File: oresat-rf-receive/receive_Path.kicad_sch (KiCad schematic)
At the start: 32 parts, among them J11 142-0711-201, J12 0022232021, J13 0022232021, J15 0022232041, J8 142-0711-201, U18 PAT1220-C-3DB, U23 PAT1220-C-3DB, U24 TQP3M9037, U25 PD2328J5050S2HF, U26 TQP3M9037, U27 LTC5505-1ES5, U28 SN74LVC1G32QDBVRQ1

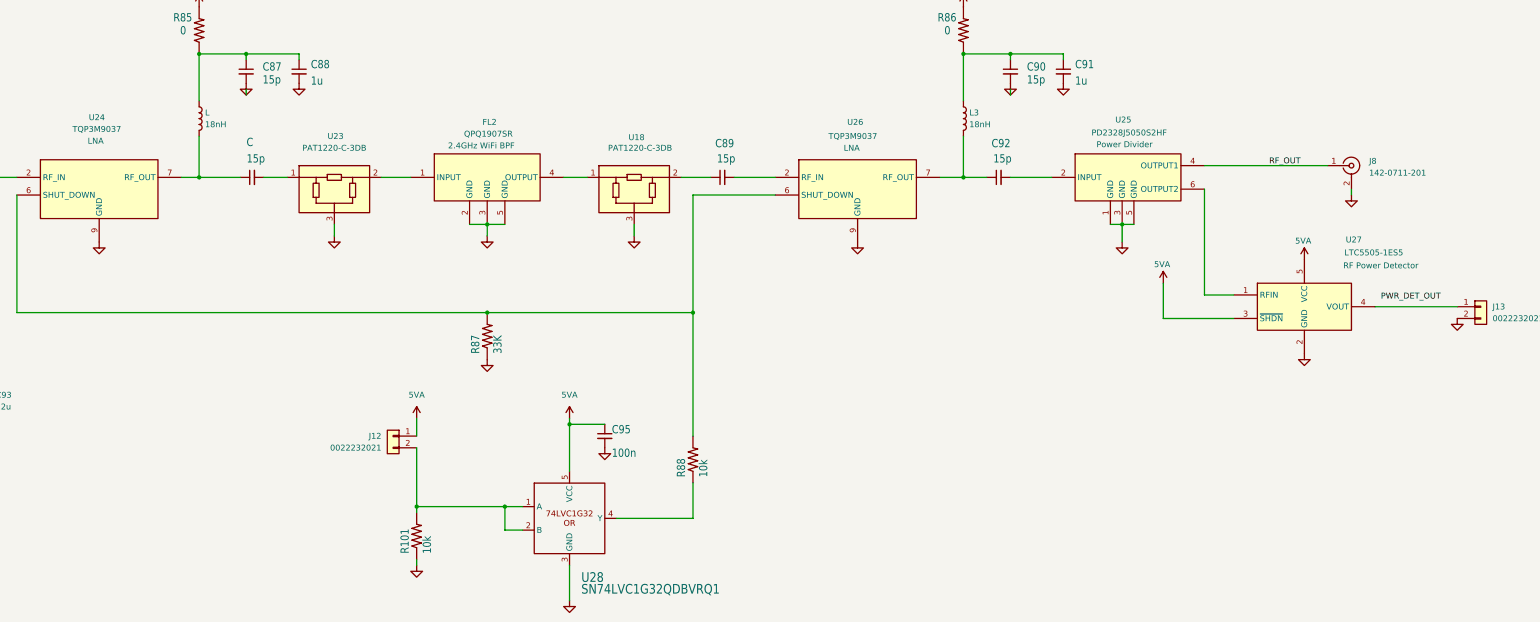
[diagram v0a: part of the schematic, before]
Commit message: updated symbol paths to oresat libraries and created pcb file
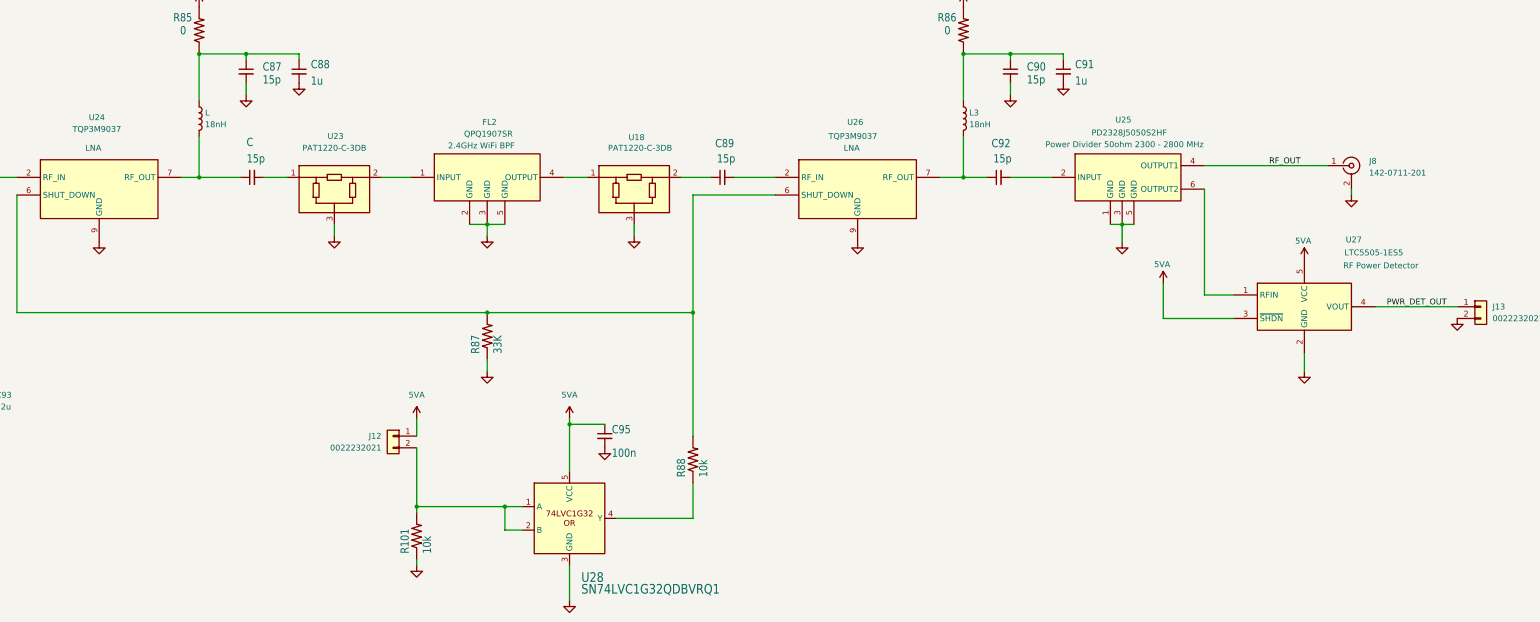
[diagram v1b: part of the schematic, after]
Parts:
- FL1: symbol QPQ1907SR:QPQ1907SR -> oresat-ics:QPQ1907SR_2.4GHz_BPF
- FL2: symbol QPQ1907SR:QPQ1907SR -> oresat-ics:QPQ1907SR_2.4GHz_BPF; MFR (none) -> Qorvo; MPN (none) -> QPQ1907SR
- U24, U26: symbol TQP3M9037:TQP3M9037 -> oresat-ics:TQP3M9037_1
- U25: symbol PD2328J5050S2HF:PD2328J5050S2HF -> oresat-ics:PD2328J5050S2HF
- U27: symbol LTC5505-1ES5#TRMPBF:LTC5505-1ES5 -> oresat-ics:LTC5505-1ES5_RF_Power_Detector
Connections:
- net PWR_DET_OUT: now also J13.1 (Pin_1), U27.4 (VOUT)

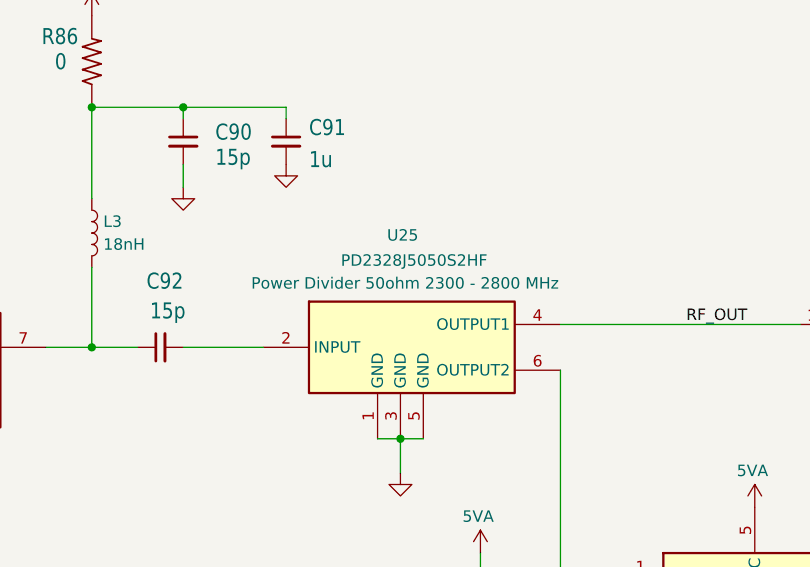
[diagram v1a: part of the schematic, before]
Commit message: Annotated schematic and added/fixed attributes
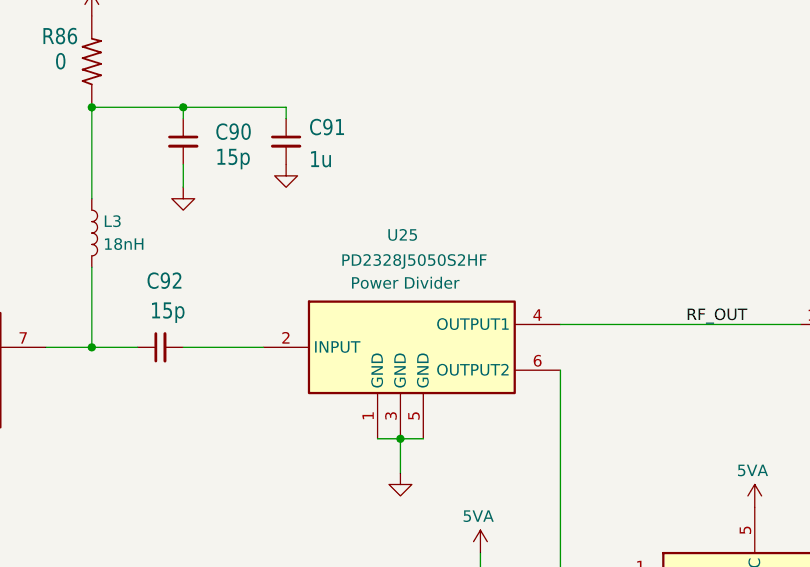
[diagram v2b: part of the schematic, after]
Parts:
- C88: Distributor DigiKey -> (none); MFR (none) -> TDK Corporation
- C91: MFR (none) -> TDK Corporation
- C94: MFR (none) -> Murata; MPN (none) -> GRM188Z71C225ME43J
- C95: Distributor DigiKey -> (none); MFR (none) -> TDK Corporation; MPN CL10B104KB8WPNC -> CGA3E2X7R1E104K080AA
- FL1: Height 0.975 -> (none)
- FL2: Height 0.975 -> (none); Manufacturer_Name Qorvo -> (none); Manufacturer_Part_Number QPQ1907SR -> (none); Mouser Part Number 772-QPQ1907SR -> (none); Mouser Price/Stock https://www.mouser.co.uk/ProductDetail/Qorvo/QPQ1907SR?qs=l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 -> (none)
- R101: Distributor DigiKey -> (none); MFR (none) -> Panasonic Electronic Components
- R88: Distributor DigiKey -> (none); MFR Panasonic Electronic Components -> Panasonic Electronic Components
- U24, U26: Height 0.95 -> (none); Mouser Part Number 772-TQP3M9037 -> (none); Mouser Price/Stock https://www.mouser.co.uk/ProductDetail/Qorvo/TQP3M9037?qs=7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 -> (none)
- U25: Height 0.58 -> (none); Mouser Part Number 620-PD2328J5050S2HF -> (none); Mouser Price/Stock https://www.mouser.co.uk/ProductDetail/Anaren/PD2328J5050S2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 -> (none)
- U27: Height 1 -> (none); Mouser Part Number 584-C5505-1ES5TRMPBF -> (none); Mouser Price/Stock https://www.mouser.co.uk/ProductDetail/Analog-Devices/LTC55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 -> (none)
- U28: Distributor DigiKey -> (none)

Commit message: Created PCB and started arranging components on receive path card
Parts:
- FL1, FL2: footprint QPQ1907SR -> oresat-ics:QPQ1907SR
- J11, J8: footprint KiCad:1420711201 -> oresat-connectors:SMA 142-0711-201
- U24, U26: footprint SON50P200X200X95-9N-D -> oresat-ics:TQP3M9037
- U25: footprint PD2328J5050S2HF -> oresat-misc:PD2328J5050S2HF
- U27: footprint SOT95P280X100-5N -> Package_TO_SOT_SMD:TSOT-23-5
- U28: footprint oresat-live-card:DBV5 -> oresat-misc:DBV5 SN74LVC1G3T2Q
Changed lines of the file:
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@@
 			)
 		)
-		(property "Footprint" "PD2328J5050S2HF"
+		(property "Footprint" "oresat-misc:PD2328J5050S2HF"
 			(at 331.47 200.33 0)
 			(effects
@@
 			)
 		)
-		(property "Footprint" "SOT95P280X100-5N"
+		(property "Footprint" "Package_TO_SOT_SMD:TSOT-23-5"
 			(at 368.3 228.27 0)
 			(effects
@@
 			)
 		)
-		(property "Footprint" "oresat-live-card:DBV5"
+		(property "Footprint" "oresat-misc:DBV5 SN74LVC1G3T2Q"
 			(at 198.12 181.61 0)
 			(effects
@@
 			)
 		)
-		(property "Footprint" "QPQ1907SR"
+		(property "Footprint" "oresat-ics:QPQ1907SR"
 			(at 58.42 200.33 0)
 			(effects
@@
 			)
 		)
-		(property "Footprint" "SON50P200X200X95-9N-D"
+		(property "Footprint" "oresat-ics:TQP3M9037"
 			(at 110.49 186.36 0)
 			(effects
@@
 			)
 		)
-		(property "Footprint" "QPQ1907SR"
+		(property "Footprint" "oresat-ics:QPQ1907SR"
 			(at 193.04 200.33 0)
 			(effects
@@
 			)
 		)
-		(property "Footprint" "SON50P200X200X95-9N-D"
+		(property "Footprint" "oresat-ics:TQP3M9037"
 			(at 274.32 186.36 0)
 			(effects
@@
 			)
 		)
-		(property "Footprint" "KiCad:1420711201"
+		(property "Footprint" "oresat-connectors:SMA 142-0711-201"
 			(at 16.51 107.95 0)
 			(effects
@@
 			)
 		)
-		(property "Footprint" "KiCad:1420711201"
+		(property "Footprint" "oresat-connectors:SMA 142-0711-201"
 			(at 367.03 105.41 0)
 			(effects

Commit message: added DPNs to BOM
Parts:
- C, C86, C87, C89, C90, C92: DPN (none) -> 490-3117-1-ND
- C88, C91: DPN (none) -> 445-173717-1-ND
- C93: DPN (none) -> 445-5723-1-ND
- C94: DPN (none) -> 490-GRM188Z71C225ME43JCT-ND; Distributor (none) -> Digi-Key
- C95: DPN (none) -> 445-5667-1-ND; Distributor (none) -> Digi-Key
- FL1, FL2: DPN (none) -> 772-QPQ1907SR; Distributor (none) -> Mouser
- J11, J8: DPN (none) -> J819-ND; Distributor (none) -> Digi-Key
- J12, J13: DPN (none) -> 900-0022232021-ND; Distributor (none) -> Digi-Key
- J15: DPN (none) -> WM4202-ND; Distributor (none) -> Digi-Key
- L, L3: DPN (none) -> 994-0603DC-18NXJRW; Distributor (none) -> Mouser
- R101, R88: DPN (none) -> P10.0KHCT-ND; Distributor (none) -> Digi-Key
- R85, R86: DPN (none) -> P0.0GCT-ND
- R87: DPN (none) -> P33KGCT-ND
- U18, U23: DPN (none) -> PAT123CT-ND; Distributor (none) -> Digi-Key
- U24, U26: DPN (none) -> 772-TQP3M9037; Distributor (none) -> Mouser
- U25: DPN (none) -> 1173-1098-1-ND; Distributor (none) -> Digi-Key
- U27: DPN (none) -> LTC5505-1ES5#TRMPBFCT-ND; Distributor (none) -> Digi-Key
- U28: DPN (none) -> 296-24202-1-ND; Distributor (none) -> Digi-Key
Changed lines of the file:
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@@
 			)
 		)
-		(property "DPN" ""
+		(property "DPN" "PAT123CT-ND"
+			(at 212.09 110.49 0)
+			(effects
+				(font
+					(size 1.27 1.27)
+				)
+				(hide yes)
+			)
+		)
+		(property "Distributor" "Digi-Key"
 			(at 212.09 110.49 0)
 			(effects
@@
 			)
 		)
-		(property "DPN" ""
+		(property "DPN" "490-GRM188Z71C225ME43JCT-ND"
 			(at 52.07 156.21 0)
 			(effects
@@
 			)
 		)
+		(property "Distributor" "Digi-Key"
+			(at 52.07 156.21 0)
+			(effects
+				(font
+					(size 1.27 1.27)
+				)
+				(hide yes)
+			)
+		)
 		(pin "1"
 		)
@@
 			)
 		)
-		(property "DPN" ""
+		(property "DPN" "490-3117-1-ND"
 			(at 293.37 85.09 0)
 			(effects
@@
 			)
 		)
-		(property "DPN" ""
+		(property "DPN" "PAT123CT-ND"
+			(at 147.32 110.49 0)
+			(effects
+				(font
+					(size 1.27 1.27)
+				)
+				(hide yes)
+			)
+		)
+		(property "Distributor" "Digi-Key"
 			(at 147.32 110.49 0)
 			(effects
@@
 			)
 		)
-		(property "DPN" ""
+		(property "DPN" "445-173717-1-ND"
 			(at 304.8 85.09 0)
 			(effects
@@
 			)
 		)
-		(property "DPN" ""
+		(property "DPN" "490-3117-1-ND"
 			(at 68.58 107.95 0)
 			(effects
@@
 			)
 		)
-		(property "DPN" ""
+		(property "DPN" "490-3117-1-ND"
 			(at 231.14 107.95 0)
 			(effects
@@
 			)
 		)
-		(property "DPN" ""
+		(property "DPN" "P33KGCT-ND"
 			(at 180.34 142.24 0)
 			(effects
@@
 			)
 		)
-		(property "DPN" ""
+		(property "DPN" "1173-1098-1-ND"
+			(at 302.26 105.41 0)
+			(effects
+				(font
+					(size 1.27 1.27)
+				)
+				(hide yes)
+			)
+		)
+		(property "Distributor" "Digi-Key"
 			(at 302.26 105.41 0)
 			(effects
@@
 			)
 		)
-		(property "DPN" ""
+		(property "DPN" "490-3117-1-ND"
 			(at 129.54 107.95 0)
 			(effects
@@
 			)
 		)
-		(property "DPN" ""
+		(property "DPN" "445-5723-1-ND"
 			(at 71.12 156.21 0)
 			(effects
@@
 			)
 		)
-		(property "DPN" ""
+		(property "DPN" "LTC5505-1ES5#TRMPBFCT-ND"
+			(at 341.63 133.35 0)
+			(effects
+				(font
+					(size 1.27 1.27)
+				)
+				(hide yes)
+			)
+		)
+		(property "Distributor" "Digi-Key"
 			(at 341.63 133.35 0)
 			(effects
@@
 			)
 		)
-		(property "DPN" ""
+		(property "DPN" "P0.0GCT-ND"
 			(at 283.21 76.2 0)
 			(effects
@@
 			)
 		)
-		(property "DPN" ""
+		(property "DPN" "994-0603DC-18NXJRW"
+			(at 283.21 95.25 0)
+			(effects
+				(font
+					(size 1.27 1.27)
+				)
+				(hide yes)
+			)
+		)
+		(property "Distributor" "Mouser"
 			(at 283.21 95.25 0)
 			(effects
@@
 			)
 		)
-		(property "DPN" ""
+		(property "DPN" "490-3117-1-ND"
 			(at 290.83 107.95 0)
 			(effects
@@
 			)
 		)
-		(property "DPN" ""
+		(property "DPN" "445-173717-1-ND"
 			(at 139.7 85.09 0)
 			(effects
@@
 			)
 		)
-		(property "Distributor" ""
+		(property "Distributor" "Digi-Key"
 			(at 198.12 181.61 0)
 			(effects
@@
 			)
 		)
-		(property "DPN" ""
+		(property "DPN" "296-24202-1-ND"
 			(at 198.12 181.61 0)
 			(effects
@@
 			)
 		)
-		(property "Distributor" ""
+		(property "Distributor" "Digi-Key"
 			(at 205.74 163.83 0)
 			(effects
@@
 			)
 		)
-		(property "DPN" ""
+		(property "DPN" "445-5667-1-ND"
 			(at 205.74 163.83 0)
 			(effects
@@
 			)
 		)
-		(property "DPN" ""
+		(property "DPN" "994-0603DC-18NXJRW"
+			(at 118.11 95.25 0)
+			(effects
+				(font
+					(size 1.27 1.27)
+				)
+				(hide yes)
+			)
+		)
+		(property "Distributor" "Mouser"
 			(at 118.11 95.25 0)
 			(effects
@@
 			)
 		)
-		(property "DPN" ""
+		(property "DPN" "772-QPQ1907SR"
+			(at 29.21 105.41 0)
+			(effects
+				(font
+					(size 1.27 1.27)
+				)
+				(hide yes)
+			)
+		)
+		(property "Distributor" "Mouser"
 			(at 29.21 105.41 0)
 			(effects
@@
 			)
 		)
-		(property "DPN" ""
+		(property "DPN" "P0.0GCT-ND"
 			(at 118.11 76.2 0)
 			(effects
@@
 			)
 		)
-		(property "Distributor" ""
+		(property "Distributor" "Digi-Key"
 			(at 224.79 168.91 0)
 			(effects
@@
 			)
 		)
-		(property "DPN" ""
+		(property "DPN" "P10.0KHCT-ND"
 			(at 224.79 168.91 0)
 			(effects
@@
 			)
 		)
-		(property "DPN" ""
+		(property "DPN" "772-TQP3M9037"
+			(at 78.74 91.44 0)
+			(effects
+				(font
+					(size 1.27 1.27)
+				)
+				(hide yes)
+			)
+		)
+		(property "Distributor" "Mouser"
 			(at 78.74 91.44 0)
 			(effects
@@
 			)
 		)
-		(property "Distributor" ""
+		(property "Distributor" "Digi-Key"
 			(at 165.1 185.42 0)
 			(effects
@@
 			)
 		)
-		(property "DPN" ""
+		(property "DPN" "P10.0KHCT-ND"
 			(at 165.1 185.42 0)
 			(effects
@@
 			)
 		)
-		(property "DPN" ""
+		(property "DPN" "772-QPQ1907SR"
+			(at 163.83 105.41 0)
+			(effects
+				(font
+					(size 1.27 1.27)
+				)
+				(hide yes)
+			)
+		)
+		(property "Distributor" "Mouser"
 			(at 163.83 105.41 0)
 			(effects
@@
 			)
 		)
-		(property "DPN" ""
+		(property "DPN" "900-0022232021-ND"
+			(at 160.02 163.83 0)
+			(effects
+				(font
+					(size 1.27 1.27)
+				)
+				(hide yes)
+			)
+		)
+		(property "Distributor" "Digi-Key"
 			(at 160.02 163.83 0)
 			(effects
@@
 			)
 		)
-		(property "DPN" ""
+		(property "DPN" "900-0022232021-ND"
+			(at 394.97 135.89 0)
+			(effects
+				(font
+					(size 1.27 1.27)
+				)
+				(hide yes)
+			)
+		)
+		(property "Distributor" "Digi-Key"
 			(at 394.97 135.89 0)
 			(effects
@@
 			)
 		)
-		(property "DPN" ""
+		(property "DPN" "772-TQP3M9037"
+			(at 242.57 91.44 0)
+			(effects
+				(font
+					(size 1.27 1.27)
+				)
+				(hide yes)
+			)
+		)
+		(property "Distributor" "Mouser"
 			(at 242.57 91.44 0)
 			(effects
@@
 			)
 		)
-		(property "DPN" ""
+		(property "DPN" "WM4202-ND"
+			(at 31.75 149.86 0)
+			(effects
+				(font
+					(size 1.27 1.27)
+				)
+				(hide yes)
+			)
+		)
+		(property "Distributor" "Digi-Key"
 			(at 31.75 149.86 0)
 			(effects
@@
 			)
 		)
-		(property "DPN" ""
+		(property "DPN" "490-3117-1-ND"
 			(at 128.27 85.09 0)
 			(effects
@@
 			)
 		)
-		(property "DPN" ""
+		(property "DPN" "J819-ND"
+			(at 16.51 107.95 0)
+			(effects
+				(font
+					(size 1.27 1.27)
+				)
+				(hide yes)
+			)
+		)
+		(property "Distributor" "Digi-Key"
 			(at 16.51 107.95 0)
 			(effects
@@
 			)
 		)
-		(property "DPN" ""
+		(property "DPN" "J819-ND"
+			(at 367.03 105.41 0)
+			(effects
+				(font
+					(size 1.27 1.27)
+				)
+				(hide yes)
+			)
+		)
+		(property "Distributor" "Digi-Key"
 			(at 367.03 105.41 0)
 			(effects
